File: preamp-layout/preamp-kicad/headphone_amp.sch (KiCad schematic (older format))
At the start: 23 parts, among them J72 Conn_01x04_Male, J73 Conn_01x03_Male, J74 Conn_01x03_Male, J75 Conn_01x03_Male, J76 Conn_01x03_Female, J77 Conn_01x04_Female, U20 TPA6120

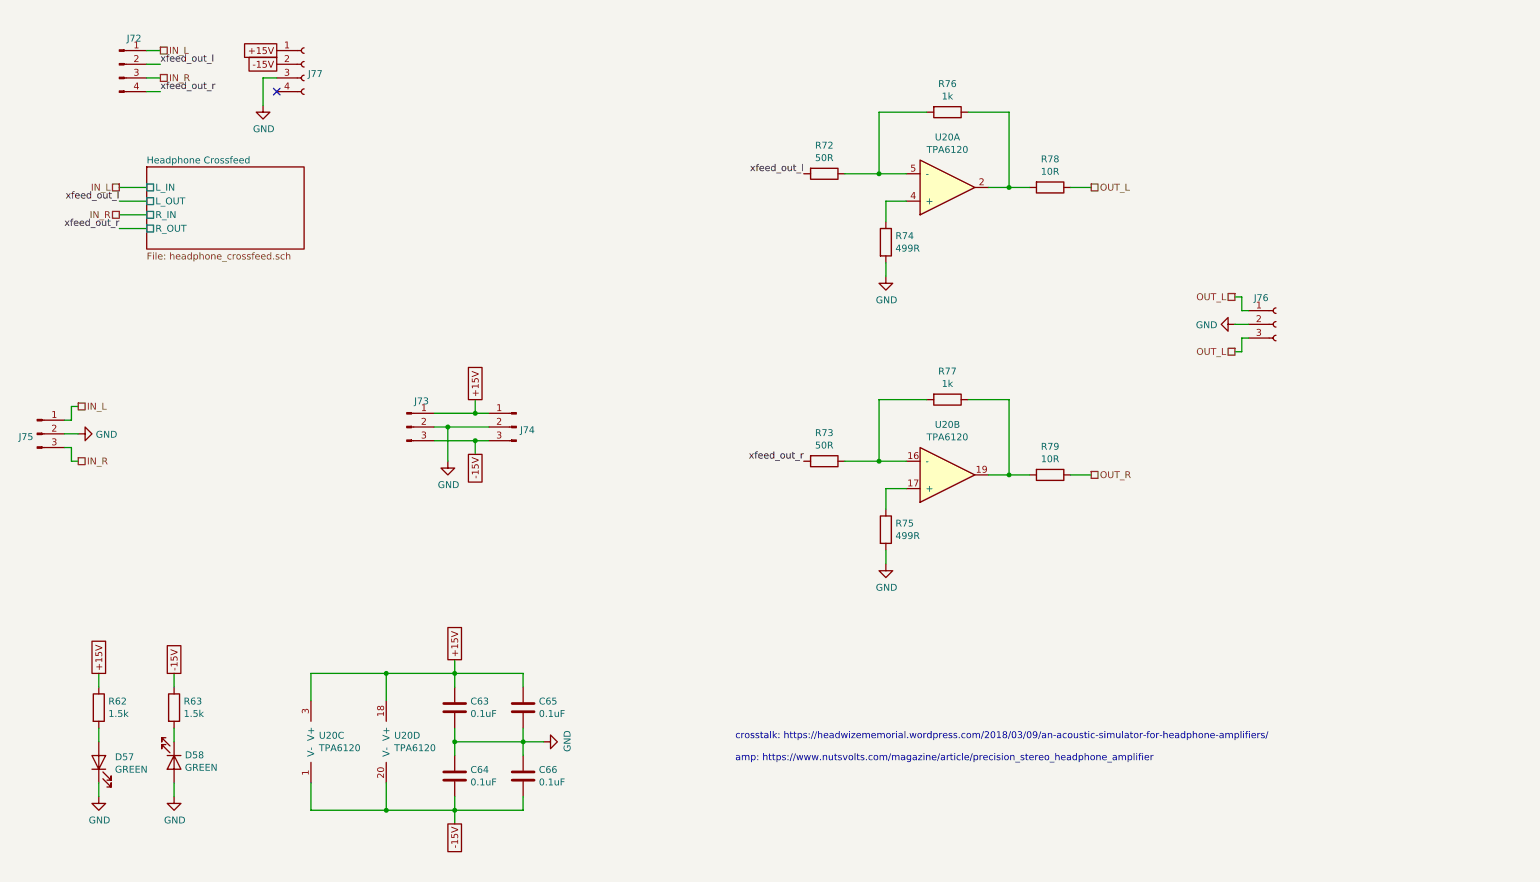
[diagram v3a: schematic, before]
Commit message: Minor Updates
Moved headphone jack to amp pcb. I2C pin updates. Added caps to LED light strip. Added 0.1uF caps to all ICs.
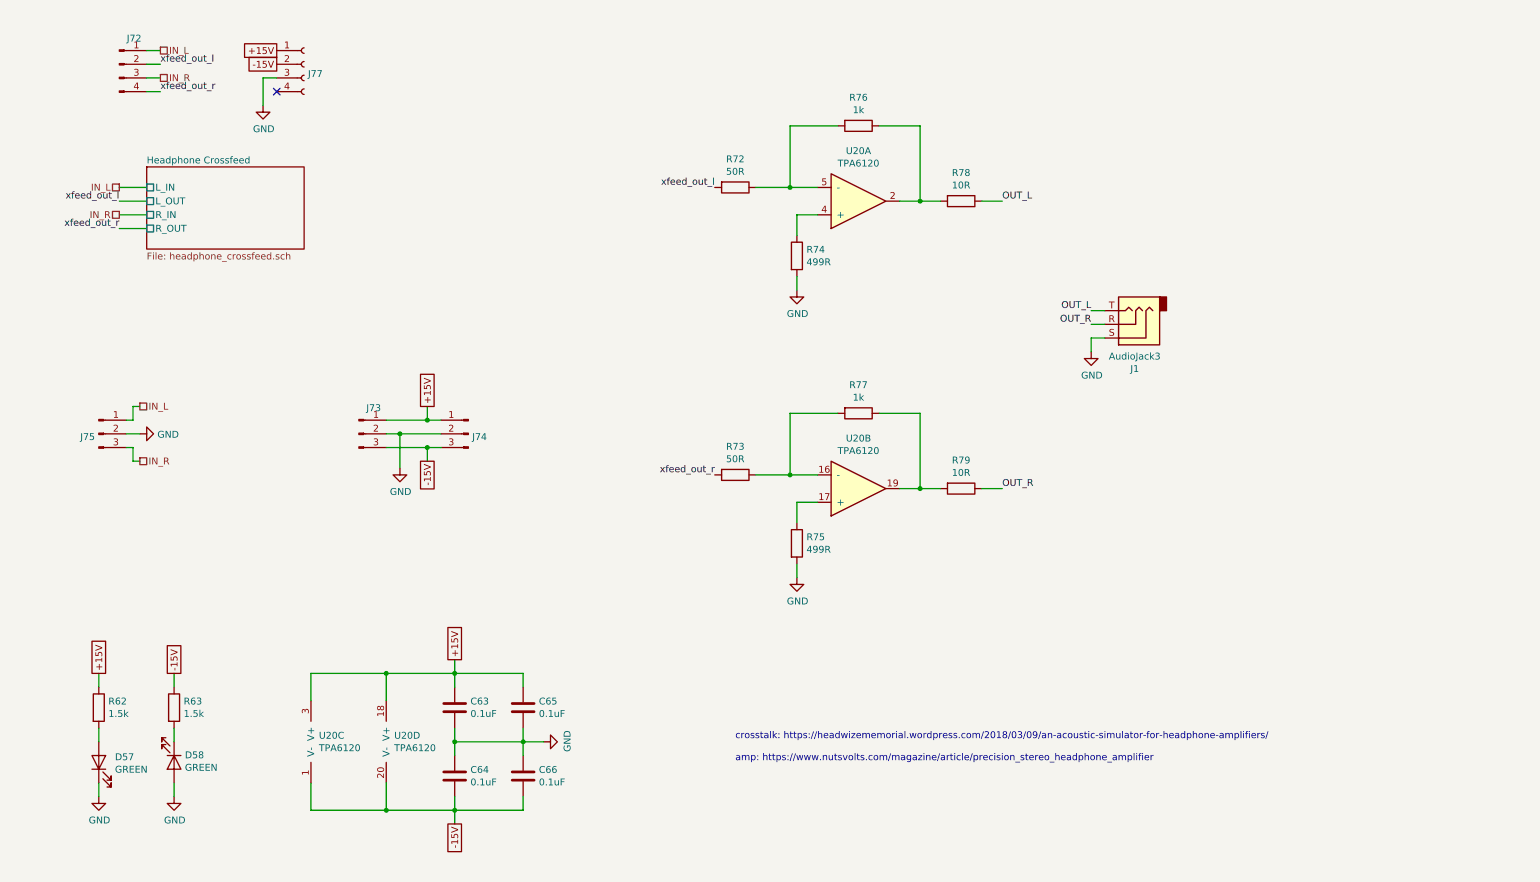
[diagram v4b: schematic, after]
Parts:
- removed J76: Conn_01x03_Female, Connector_PinHeader_2.54mm:PinHeader_1x03_P2.54mm_Vertical, symbol Connector:Conn_01x03_Female
- added J1: AudioJack3, symbol Connector:AudioJack3
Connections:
- net GND: now also J1.S
- net OUT_L: now also J1.T
- net OUT_R: now also J1.R
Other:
- moved on the sheet: J73, J74, J75, R72, R73, R74, R75, R76, R77, R78, R79, U20A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

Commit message: RefDes Update
Re-ran refdes assignment, updated BOM accordingly.
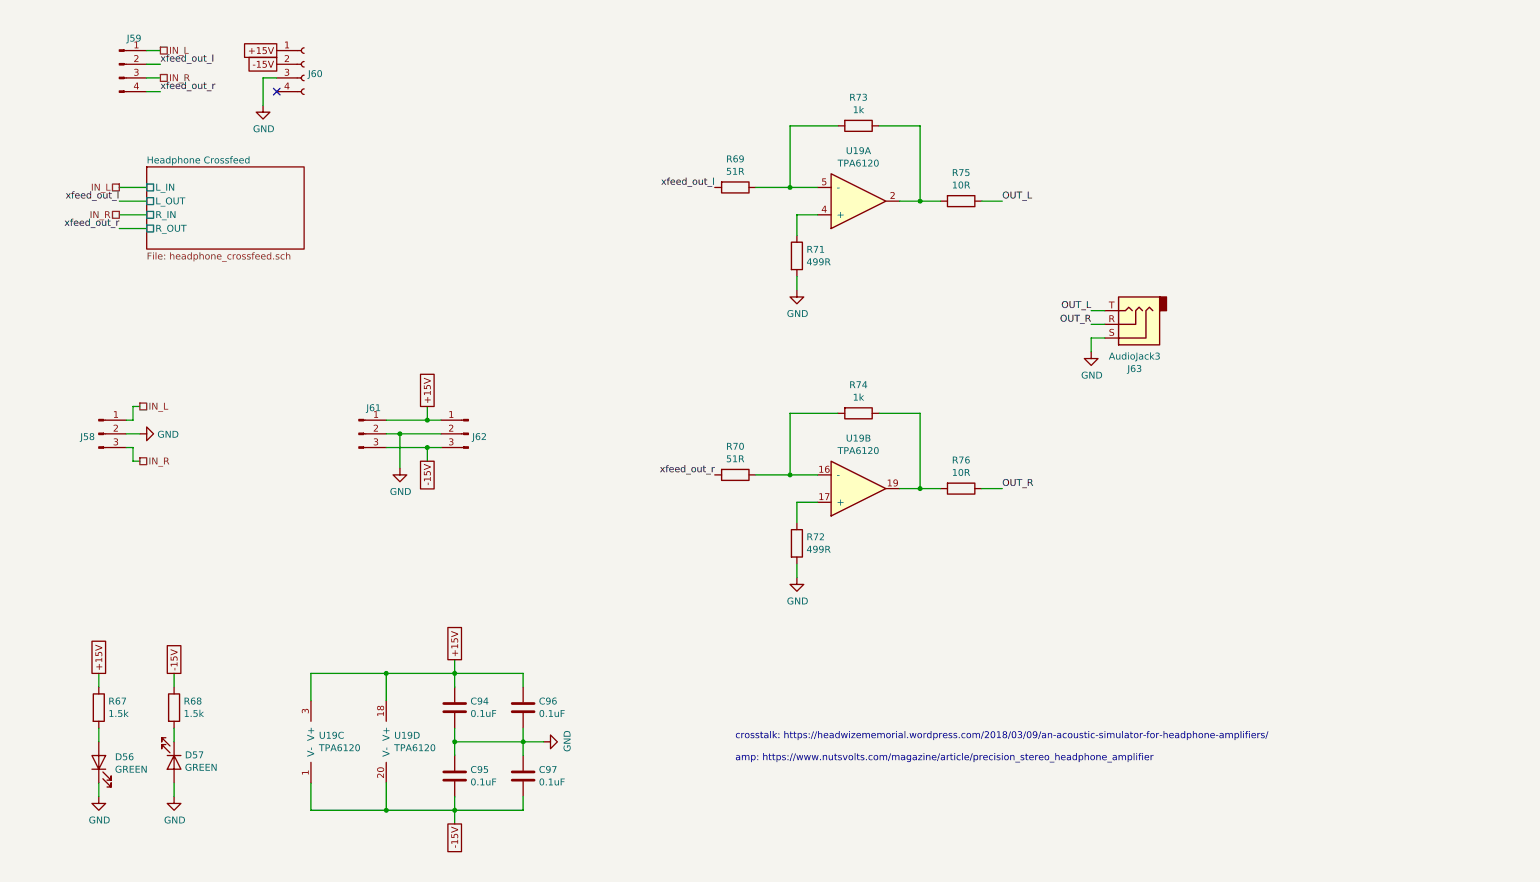
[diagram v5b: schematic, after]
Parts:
- R69: renamed from R72; value 50R -> 51R
- R70: renamed from R73; value 50R -> 51R
- renumbered C63 to C94, C64 to C95, C65 to C96, C66 to C97, D57 to D56, D58 to D57, J75 to J58, J72 to J59, J77 to J60, J73 to J61, J74 to J62, J1 to J63, R62 to R67, R63 to R68, R74 to R71, R75 to R72, R76 to R73, R77 to R74, R78 to R75, R79 to R76, U20 to U19

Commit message: Periodic backup
Extensive changes as a result of PCB layout phase.
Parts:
- removed C96, C97: 0.1uF, Capacitor_SMD:C_0805_2012Metric_Pad1.15x1.40mm_HandSolder, symbol Device:C
- removed J59: Conn_01x04_Male, Connector_PinHeader_2.54mm:PinHeader_1x04_P2.54mm_Vertical, symbol Connector:Conn_01x04_Male
- removed J60: Conn_01x04_Female, Connector_PinHeader_2.54mm:PinHeader_1x04_P2.54mm_Vertical, symbol Connector:Conn_01x04_Female
- removed J63: AudioJack3, symbol Connector:AudioJack3
- added C96, C97: 100uF, Capacitor_SMD:CP_Elec_8x6.2, symbol Device:CP1
- added J32: Conn_01x03_Male, Connector_JST:JST_EH_B3B-EH-A_1x03_P2.50mm_Vertical, symbol Connector:Conn_01x03_Male
- added J35: Conn_01x05_Male, Connector_PinHeader_2.54mm:PinHeader_1x05_P2.54mm_Vertical, symbol Connector:Conn_01x05_Male
- J58: footprint Connector_PinHeader_2.54mm:PinHeader_1x03_P2.54mm_Vertical -> Connector_JST:JST_EH_B3B-EH-A_1x03_P2.50mm_Vertical
- J61, J62: footprint Connector_JST:JST_EH_B3B-EH-A_1x03_P2.50mm_Vertical -> Connector_JST:JST_EH_S3B-EH_1x03_P2.50mm_Horizontal
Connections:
- net +15V: now also C96.1
- net -15V: now also C97.2
- net GND: now also C96.2, C97.1, J32.3 (Pin_3), J35.5 (Pin_5)
- net IN_L: now also J35.1 (Pin_1)
- net IN_R: now also J35.3 (Pin_3)
- net OUT_L: now also J32.1 (Pin_1)
- net OUT_R: now also J32.2 (Pin_2)
- net xfeed_out_l: now also J35.2 (Pin_2)
- net xfeed_out_r: now also J35.4 (Pin_4)
- no-connect marks 1 -> 0
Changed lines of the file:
@@
 $Descr A4 11693 8268
 encoding utf-8
-Sheet 10 13
+Sheet 9 13
 Title "Headphone Amplifier Board"
 Date "2020-02-25"
@@
 Text Notes 6550 6450 0    50   ~ 0
 crosstalk: https://headwizememorial.wordpress.com/2018/03/09/an-acoustic-simulator-for-headphone-amplifiers/\n\namp: https://www.nutsvolts.com/magazine/article/precision_stereo_headphone_amplifier
-Wire Wire Line
-	3100 1450 3100 1650
-$Comp
-L power:GND #PWR?
-U 1 1 5EF0112C
-P 3100 1650
-AR Path="/6009D432/5EF0112C" Ref="#PWR?"  Part="1"
-AR Path="/5E4A803E/5EF0112C" Ref="#PWR091"  Part="1"
-F 0 "#PWR091" H 3100 1400 50  0001 C CNN
-F 1 "GND" H 3105 1477 50  0000 C CNN
-F 2 "" H 3100 1650 50  0001 C CNN
-F 3 "" H 3100 1650 50  0001 C CNN
-	1    3100 1650
-	1    0    0    -1
-$EndComp
 Text Label 6400 2250 2    50   ~ 0
 xfeed_out_l
@@
 F 0 "J61" H 3908 4239 50  0000 C CNN
 F 1 "Conn_01x03_Male" H 3772 3983 50  0001 R CNN
-F 2 "Connector_JST:JST_EH_B3B-EH-A_1x03_P2.50mm_Vertical" H 3800 4050 50  0001 C CNN
+F 2 "Connector_JST:JST_EH_S3B-EH_1x03_P2.50mm_Horizontal" H 3800 4050 50  0001 C CNN
 F 3 "~" H 3800 4050 50  0001 C CNN
 	1    3800 4050
@@
 	1    0    0    -1
 $EndComp
-NoConn ~ 3200 1550
 $Comp
 L preamp:TPA6120 U19
@@
 F 0 "J62" H 4572 4028 50  0000 R CNN
 F 1 "Conn_01x03_Male" H 4572 3983 50  0001 R CNN
-F 2 "Connector_JST:JST_EH_B3B-EH-A_1x03_P2.50mm_Vertical" H 4600 4050 50  0001 C CNN
+F 2 "Connector_JST:JST_EH_S3B-EH_1x03_P2.50mm_Horizontal" H 4600 4050 50  0001 C CNN
 F 3 "~" H 4600 4050 50  0001 C CNN
 	1    4600 4050
 	-1   0    0    -1
-$EndComp
-$Comp
-L Connector:Conn_01x04_Female J60
-U 1 1 5EF5CC6D
-P 3400 1350
-F 0 "J60" H 3428 1280 50  0000 L CNN
-F 1 "Conn_01x04_Female" H 3428 1235 50  0001 L CNN
-F 2 "Connector_PinHeader_2.54mm:PinHeader_1x04_P2.54mm_Vertical" H 3400 1350 50  0001 C CNN
-F 3 "~" H 3400 1350 50  0001 C CNN
-	1    3400 1350
-	1    0    0    -1
-$EndComp
-$Comp
-L Device:C C96
-U 1 1 5EF7CEF2
-P 5000 6050
-F 0 "C96" H 5115 6096 50  0000 L CNN
-F 1 "0.1uF" H 5115 6005 50  0000 L CNN
-F 2 "Capacitor_SMD:C_0805_2012Metric_Pad1.15x1.40mm_HandSolder" H 5038 5900 50  0001 C CNN
-F 3 "~" H 5000 6050 50  0001 C CNN
-	1    5000 6050
-	1    0    0    -1
-$EndComp
-$Comp
-L Device:C C97
-U 1 1 5EF8629D
-P 5000 6550
-F 0 "C97" H 5115 6596 50  0000 L CNN
-F 1 "0.1uF" H 5115 6505 50  0000 L CNN
-F 2 "Capacitor_SMD:C_0805_2012Metric_Pad1.15x1.40mm_HandSolder" H 5038 6400 50  0001 C CNN
-F 3 "~" H 5000 6550 50  0001 C CNN
-	1    5000 6550
-	1    0    0    -1
 $EndComp
 $Comp
@@
 F 0 "J58" H 1872 4028 50  0000 R CNN
 F 1 "Conn_01x03_Male" H 1872 3983 50  0001 R CNN
-F 2 "Connector_PinHeader_2.54mm:PinHeader_1x03_P2.54mm_Vertical" H 1900 4050 50  0001 C CNN
+F 2 "Connector_JST:JST_EH_B3B-EH-A_1x03_P2.50mm_Vertical" H 1900 4050 50  0001 C CNN
 F 3 "~" H 1900 4050 50  0001 C CNN
 	1    1900 4050
@@
 -15V
 Wire Wire Line
-	4500 5800 5000 5800
-Wire Wire Line
-	5000 5800 5000 5900
-Wire Wire Line
-	4500 6800 5000 6800
-Wire Wire Line
-	5000 6800 5000 6700
-Wire Wire Line
-	4500 6200 4500 6300
-Connection ~ 4500 6300
-Wire Wire Line
-	4500 6300 4500 6400
-Wire Wire Line
-	5000 6200 5000 6300
-Wire Wire Line
-	4500 6300 5000 6300
-Connection ~ 5000 6300
-Wire Wire Line
-	5000 6300 5000 6400
-Wire Wire Line
 	4500 5700 4500 5800
 Connection ~ 4500 5800
@@
 Wire Wire Line
 	4500 6800 4500 6900
-$Comp
-L Connector:Conn_01x04_Male J59
-U 1 1 5E6D1CB1
-P 2050 1350
-F 0 "J59" H 2158 1539 50  0000 C CNN
-F 1 "Conn_01x04_Male" H 2158 1540 50  0001 C CNN
-F 2 "Connector_PinHeader_2.54mm:PinHeader_1x04_P2.54mm_Vertical" H 2050 1350 50  0001 C CNN
-F 3 "~" H 2050 1350 50  0001 C CNN
-	1    2050 1350
-	1    0    0    -1
-$EndComp
-Text GLabel 3200 1250 0    50   UnSpc ~ 0
-+15V
-Text GLabel 3200 1350 0    50   UnSpc ~ 0
--15V
 Text HLabel 2050 2250 0    50   UnSpc ~ 0
 IN_L
@@
 F5 "R_OUT" U L 2250 2550 50
 $EndSheet
-Wire Wire Line
-	3200 1450 3100 1450
 Text GLabel 4300 3850 1    50   UnSpc ~ 0
 +15V
@@
 Wire Wire Line
 	4000 5800 3450 5800
-Text HLabel 2350 1250 2    50   UnSpc ~ 0
+Text HLabel 1850 1100 2    50   UnSpc ~ 0
 IN_L
-Text HLabel 2350 1450 2    50   UnSpc ~ 0
+Text HLabel 1850 1300 2    50   UnSpc ~ 0
 IN_R
-Text Label 2350 1350 0    50   ~ 0
+Text Label 1850 1200 0    50   ~ 0
 xfeed_out_l
-Text Label 2350 1550 0    50   ~ 0
+Text Label 1850 1400 0    50   ~ 0
 xfeed_out_r
 Wire Wire Line
-	2250 1250 2350 1250
-Wire Wire Line
-	2250 1350 2350 1350
-Wire Wire Line
-	2250 1450 2350 1450
-Wire Wire Line
-	2250 1550 2350 1550
+	1750 1100 1850 1100
+Wire Wire Line
+	1750 1200 1850 1200
+Wire Wire Line
+	1750 1300 1850 1300
+Wire Wire Line
+	1750 1400 1850 1400
 Wire Wire Line
 	2050 2250 2250 2250
@@
 Wire Wire Line
 	4300 3950 4400 3950
-Wire Wire Line
-	5000 6300 5150 6300
-$Comp
-L Connector:AudioJack3 J63
-U 1 1 5E7B4943
-P 9450 3250
-AR Path="/5E4A803E/5E7B4943" Ref="J63"  Part="1"
-AR Path="/5E7B4943" Ref="J?"  Part="1"
-F 0 "J63" H 9432 3575 50  0000 C CNN
-F 1 "AudioJack3" H 9432 3484 50  0000 C CNN
-F 2 "" H 9450 3250 50  0001 C CNN
-F 3 "~" H 9450 3250 50  0001 C CNN
-	1    9450 3250
-	-1   0    0    1
-$EndComp
 $Comp
 L power:GND #PWR?
@@
 Text Label 8500 4450 0    50   ~ 0
 OUT_R
+$Comp
+L Connector:Conn_01x03_Male J?
+U 1 1 5F30CFBF
+P 9450 3250
+AR Path="/5E27B612/5F30CFBF" Ref="J?"  Part="1"
+AR Path="/6009D432/5F30CFBF" Ref="J?"  Part="1"
+AR Path="/5E4A803E/5F30CFBF" Ref="J32"  Part="1"
+F 0 "J32" H 9422 3228 50  0000 R CNN
+F 1 "Conn_01x03_Male" H 9422 3183 50  0001 R CNN
+F 2 "Connector_JST:JST_EH_B3B-EH-A_1x03_P2.50mm_Vertical" H 9450 3250 50  0001 C CNN
+F 3 "~" H 9450 3250 50  0001 C CNN
+	1    9450 3250
+	-1   0    0    -1
+$EndComp
+$Comp
+L Device:CP1 C96
+U 1 1 5F332D1E
+P 5000 6050
+F 0 "C96" H 5115 6096 50  0000 L CNN
+F 1 "100uF" H 5115 6005 50  0000 L CNN
+F 2 "Capacitor_SMD:CP_Elec_8x6.2" H 5000 6050 50  0001 C CNN
+F 3 "~" H 5000 6050 50  0001 C CNN
+	1    5000 6050
+	1    0    0    -1
+$EndComp
+$Comp
+L Device:CP1 C97
+U 1 1 5F3373CD
+P 5000 6550
+F 0 "C97" H 5115 6596 50  0000 L CNN
+F 1 "100uF" H 5115 6505 50  0000 L CNN
+F 2 "Capacitor_SMD:CP_Elec_8x6.2" H 5000 6550 50  0001 C CNN
+F 3 "~" H 5000 6550 50  0001 C CNN
+	1    5000 6550
+	1    0    0    -1
+$EndComp
+Wire Wire Line
+	4500 6200 4500 6300
+Wire Wire Line
+	4500 5800 5000 5800
+Wire Wire Line
+	5000 5800 5000 5900
+Wire Wire Line
+	4500 6800 5000 6800
+Wire Wire Line
+	5000 6800 5000 6700
+Wire Wire Line
+	4500 6300 5000 6300
+Connection ~ 4500 6300
+Wire Wire Line
+	4500 6300 4500 6400
+Wire Wire Line
+	5000 6200 5000 6300
+Connection ~ 5000 6300
+Wire Wire Line
+	5000 6300 5150 6300
+Wire Wire Line
+	5000 6300 5000 6400
+$Comp
+L Connector:Conn_01x05_Male J35
+U 1 1 5F415EA4
+P 1550 1300
+F 0 "J35" H 1658 1589 50  0000 C CNN
+F 1 "Conn_01x05_Male" H 1658 1590 50  0001 C CNN
+F 2 "Connector_PinHeader_2.54mm:PinHeader_1x05_P2.54mm_Vertical" H 1550 1300 50  0001 C CNN
+F 3 "~" H 1550 1300 50  0001 C CNN
+	1    1550 1300
+	1    0    0    -1
+$EndComp
+$Comp
+L power:GND #PWR?
+U 1 1 5F41D7DE
+P 1850 1600
+AR Path="/6009D432/5F41D7DE" Ref="#PWR?"  Part="1"
+AR Path="/5E4A803E/5F41D7DE" Ref="#PWR045"  Part="1"
+F 0 "#PWR045" H 1850 1350 50  0001 C CNN
+F 1 "GND" H 1855 1427 50  0000 C CNN
+F 2 "" H 1850 1600 50  0001 C CNN
+F 3 "" H 1850 1600 50  0001 C CNN
+	1    1850 1600
+	1    0    0    -1
+$EndComp
+Wire Wire Line
+	1850 1500 1850 1600
+Wire Wire Line
+	1750 1500 1850 1500
 $EndSCHEMATC

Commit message: PCB layout
trying a different layout for the gain stage board, this serves as a reference point.
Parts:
- C94, C95: footprint Capacitor_SMD:C_0805_2012Metric_Pad1.15x1.40mm_HandSolder -> Capacitor_SMD:C_1206_3216Metric_Pad1.42x1.75mm_HandSolder
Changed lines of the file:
@@
 F 0 "C95" H 4385 6504 50  0000 R CNN
 F 1 "0.1uF" H 4385 6595 50  0000 R CNN
-F 2 "Capacitor_SMD:C_0805_2012Metric_Pad1.15x1.40mm_HandSolder" H 4538 6400 50  0001 C CNN
+F 2 "Capacitor_SMD:C_1206_3216Metric_Pad1.42x1.75mm_HandSolder" H 4538 6400 50  0001 C CNN
 F 3 "~" H 4500 6550 50  0001 C CNN
 	1    4500 6550
@@
 F 0 "C94" H 4615 6096 50  0000 L CNN
 F 1 "0.1uF" H 4615 6005 50  0000 L CNN
-F 2 "Capacitor_SMD:C_0805_2012Metric_Pad1.15x1.40mm_HandSolder" H 4538 5900 50  0001 C CNN
+F 2 "Capacitor_SMD:C_1206_3216Metric_Pad1.42x1.75mm_HandSolder" H 4538 5900 50  0001 C CNN
 F 3 "~" H 4500 6050 50  0001 C CNN
 	1    4500 6050

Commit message: PCB layout
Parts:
- removed J61, J62: Conn_01x03_Male, Connector_JST:JST_EH_S3B-EH_1x03_P2.50mm_Horizontal, symbol Connector:Conn_01x03_Male
- added J47, J48: Conn_01x04_Male, Connector_JST:JST_EH_S4B-EH_1x04_P2.50mm_Horizontal, symbol Connector:Conn_01x04_Male
- R71, R72: value 499R -> 1k
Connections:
- net +15V: now also J47.1 (Pin_1), J48.1 (Pin_1)
- net -15V: now also J47.2 (Pin_2), J48.2 (Pin_2)
- net GND: now also J47.3 (Pin_3), J48.3 (Pin_3)
- net at U19.4 (+): now also R69.1; no longer R71.1
- net at R73.2, U19.5 (-): now also R71.1; no longer R69.1
- net at R74.2, U19.16 (-): now also R72.1; no longer R70.1
- net at U19.17 (+): now also R70.1; no longer R72.1
- new net +5V: J47.4 (Pin_4), J48.4 (Pin_4)
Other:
- note added: "crosstalk: https://headwizememorial.wordpress.com/2018/03/09/an-acoustic-simulator-for-headphone-amplifiers/\n\namp: http://www.pavouk.org/hw/tpa6120headamp/en_index.html"
- note removed: "crosstalk: https://headwizememorial.wordpress.com/2018/03/09/an-acoustic-simulator-for-headphone-amplifiers/\n\namp: https://www.nutsvolts.com/magazine/article/precision_stereo_headphone_amplifier"
- moved on the sheet: R69, R70, R71, R72, R73, R74
